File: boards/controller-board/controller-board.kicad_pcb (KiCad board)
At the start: 2 copper layers, 130 x 115 mm, 172 parts, among them J1 Conn_01x02, J2 Conn_01x02, J3 Conn_01x02, J4 Conn_01x02, J5 Conn_01x03, J6 Conn_01x02, Q1 Goford_G11S_20V_11A, Q2 PMV45EN, SW1 EG1271, U1 CAT4201, U10 CAT4201, U11 CAT4201, U12 CAT4201, U13 CAT4201, U14 CAT4201, U15 CAT4201, U17 CAT4201, U18 CAT4201, U25 RPi_Pico, U3 LTC3624, U4 CAT4201, U5 CAT4201, U6 CAT4201, U7 MCP4728, U8 ADS1015IRUGR, U9 ADS1015IRUGR

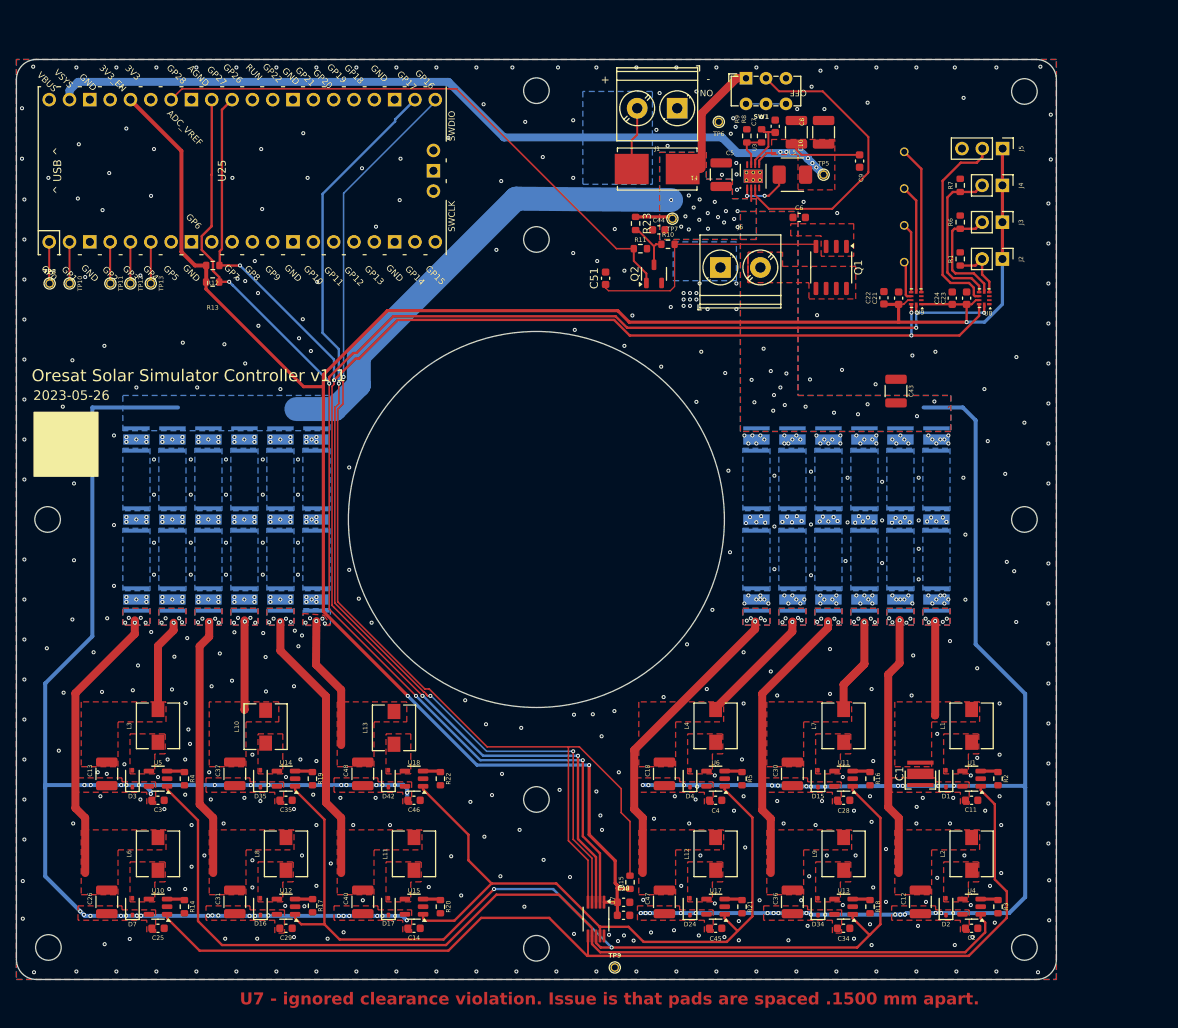
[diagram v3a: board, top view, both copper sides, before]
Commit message: redesigned pcb
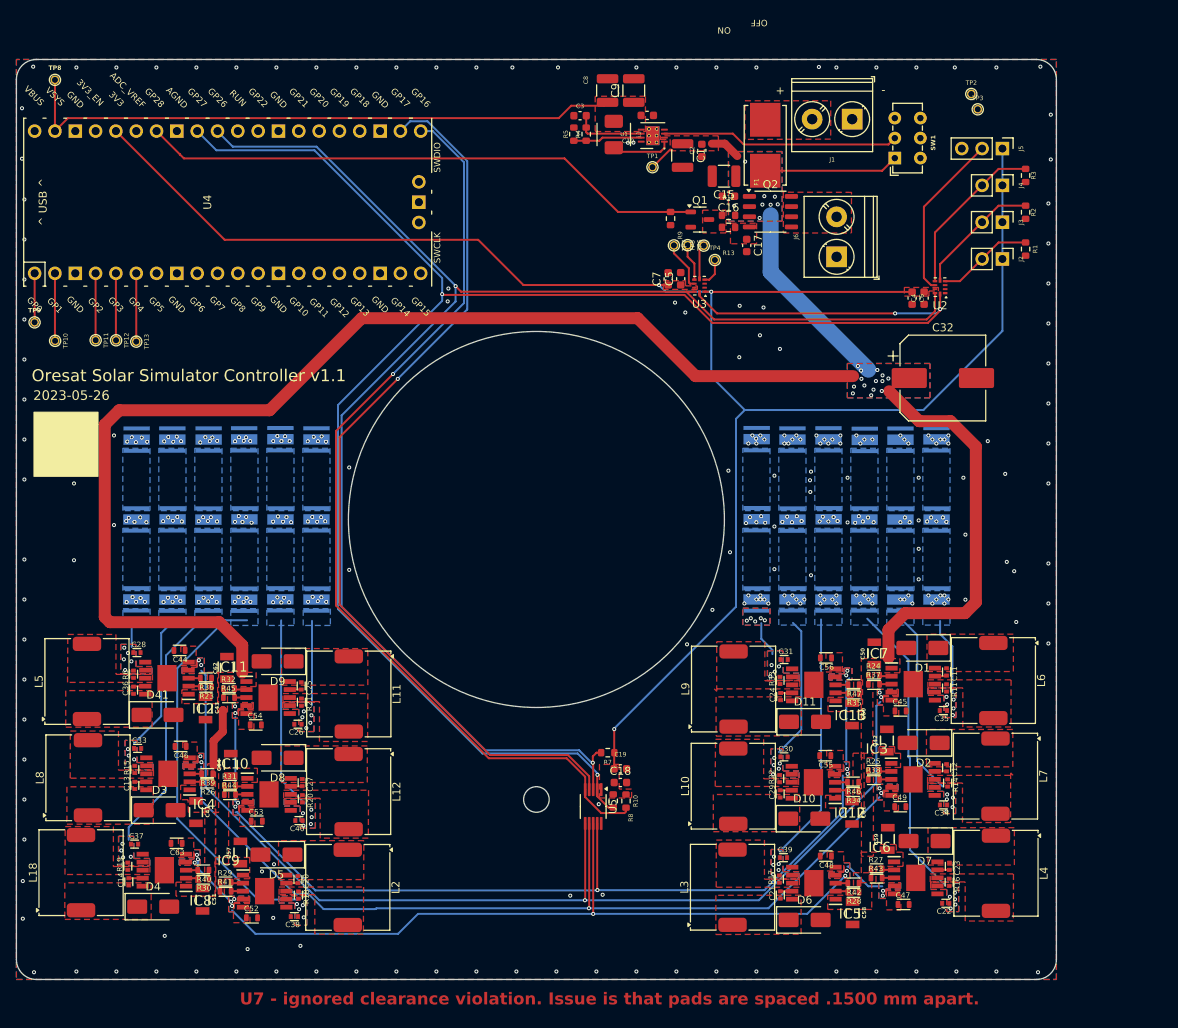
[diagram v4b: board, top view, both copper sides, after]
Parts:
- removed D12, D13, D14: XPEBGR-L1-0000-00D01, oresat-diodes:Cree-LED
- removed D15, D16, D17, D24, D34, D35, D42: NSR0320, Diode_SMD:D_SOD-323
- removed D18, D19, D20, D21: ELUA3535OGB-P6070U23240500-VD1M, oresat-diodes:Cree-LED
- removed D22, D23: NP, oresat-diodes:Cree-LED
- removed D25, D26, D27: XPEBRD-L1-0000-00501, oresat-diodes:Cree-LED
- removed D28, D29, D30, D31, D32, D33, D36, D37, D38, D39, D40: XPEBBL-L1-0000-00201, oresat-diodes:Cree-LED
- removed D43, D44, D45, D46: ELUC3535NUB-P7085Q15070100-S22Q, oresat-diodes:Cree-LED
- removed L13: 56u, Inductor_SMD:L_Wuerth_HCI-5040
- removed the REF** at (206.0, 102.5)
- removed the REF** at (206.0, 49.0)
- removed the REF** at (83.9, 102.5)
- removed the REF** at (84.0, 156.0)
- removed the REF** at (145.0, 156.1)
- removed the REF** at (145.0, 48.9)
- removed the REF** at (145.0, 67.5)
- removed the REF** at (206.0, 156.0)
- removed U10, U11, U12, U13, U14, U15, U17, U18, U6: CAT4201, Package_TO_SOT_SMD:TSOT-23-5
- removed U25: RPi_Pico, oresat-misc:RPi_Pico_TH
- removed U7: MCP4728, Package_SO:MSOP-10_3x3mm_P0.5mm
- removed U8, U9: ADS1015IRUGR, Package_DFN_QFN:Texas_R-PUQFN-N10
- added C15: 22u, Capacitor_SMD:C_1210_3225Metric, F.Cu at (168.5, 59.6)
- added C16: 1u, Capacitor_SMD:C_0603_1608Metric, F.Cu at (169.0, 62.1)
- added C17: C_Small, Capacitor_SMD:C_0603_1608Metric, F.Cu at (171.3, 68.2)
- added C27: 100n, oresat-passives:0402-C, F.Cu at (115.7, 135.4)
- added C32: 470u, Capacitor_SMD:CP_Elec_10x12.5, F.Cu at (195.8, 84.8)
- added C33: 100n, oresat-passives:0402-C, F.Cu at (95.2, 131.1)
- added C38: 100n, oresat-passives:0402-C, F.Cu at (114.7, 152.1)
- added C39: 100n, oresat-passives:0402-C, F.Cu at (175.9, 144.8)
- added C41: 10u, oresat-passives:1206-C, F.Cu at (102.5, 139.1)
- added C42: 10u, oresat-passives:1206-C, F.Cu at (188.8, 130.1)
- added C49: 1u, oresat-passives:0603-C, F.Cu at (190.5, 138.4)
- added C50: 10u, oresat-passives:1206-C, F.Cu at (187.2, 119.2)
- added C52: 1u, oresat-passives:0603-C, F.Cu at (109.4, 152.3)
- added C53: 1u, oresat-passives:0603-C, F.Cu at (110.0, 140.2)
- added C54: 1u, oresat-passives:0603-C, F.Cu at (109.9, 128.2)
- added C55: 1u, oresat-passives:0603-C, F.Cu at (181.1, 132.0)
- added C56: 1u, oresat-passives:0603-C, F.Cu at (181.2, 119.8)
- added C57: 10u, oresat-passives:1206-C, F.Cu at (108.0, 144.1)
- added C58: 10u, oresat-passives:1206-C, F.Cu at (184.5, 151.7)
- added C59: 10u, oresat-passives:1206-C, F.Cu at (188.9, 142.4)
- added C60: 10u, oresat-passives:1206-C, F.Cu at (184.5, 126.9)
- added C61: 10u, oresat-passives:1206-C, F.Cu at (184.5, 139.2)
- added C62: 10u, oresat-passives:1206-C, F.Cu at (106.3, 121.0)
- added C63: 1u, oresat-passives:0603-C, F.Cu at (100.0, 143.0)
- added C64: 10u, oresat-passives:1206-C, F.Cu at (106.8, 133.2)
- added D49: XPEBBL-L1-0000-00201, oresat-diodes:Cree-LED, B.Cu at (190.5, 112.5)
- added D50: XPEBBL-L1-0000-00201, oresat-diodes:Cree-LED, B.Cu at (190.5, 92.5)
- added D51: XPEBBL-L1-0000-00201, oresat-diodes:Cree-LED, B.Cu at (99.5, 112.5)
- added D52: XPEBBL-L1-0000-00201, oresat-diodes:Cree-LED, B.Cu at (99.5, 92.5)
- added D53: XPEBBL-L1-0000-00201, oresat-diodes:Cree-LED, B.Cu at (181.5, 112.5)
- added D54: XPEBBL-L1-0000-00201, oresat-diodes:Cree-LED, B.Cu at (181.5, 92.5)
- added D55: XPEBBL-L1-0000-00201, oresat-diodes:Cree-LED, B.Cu at (186.0, 112.5)
- added D56: XPEBBL-L1-0000-00201, oresat-diodes:Cree-LED, B.Cu at (186.1, 92.5)
- added D57: XPEBBL-L1-0000-00201, oresat-diodes:Cree-LED, B.Cu at (195.0, 112.5)
- added D58: XPEBBL-L1-0000-00201, oresat-diodes:Cree-LED, B.Cu at (195.0, 92.5)
- added D59: XPEBBL-L1-0000-00201, oresat-diodes:Cree-LED, B.Cu at (95.0, 102.5)
- added D60: XPEBBL-L1-0000-00201, oresat-diodes:Cree-LED, B.Cu at (190.5, 102.5)
- added D61: XPEBBL-L1-0000-00201, oresat-diodes:Cree-LED, B.Cu at (99.5, 102.5)
- added D62: XPEBBL-L1-0000-00201, oresat-diodes:Cree-LED, B.Cu at (181.5, 102.5)
- added D63: XPEBBL-L1-0000-00201, oresat-diodes:Cree-LED, B.Cu at (186.0, 102.5)
- added D64: XPEBBL-L1-0000-00201, oresat-diodes:Cree-LED, B.Cu at (195.0, 102.5)
- added D71: XPEBBL-L1-0000-00201, oresat-diodes:Cree-LED, B.Cu at (104.0, 112.5)
- added D72: XPEBBL-L1-0000-00201, oresat-diodes:Cree-LED, B.Cu at (104.0, 92.5)
- added D73: XPEBBL-L1-0000-00201, oresat-diodes:Cree-LED, B.Cu at (108.5, 112.5)
- added D74: XPEBBL-L1-0000-00201, oresat-diodes:Cree-LED, B.Cu at (108.5, 92.5)
- added D75: XPEBBL-L1-0000-00201, oresat-diodes:Cree-LED, B.Cu at (113.0, 112.5)
- added D76: XPEBBL-L1-0000-00201, oresat-diodes:Cree-LED, B.Cu at (113.0, 92.5)
- added D77: XPEBBL-L1-0000-00201, oresat-diodes:Cree-LED, B.Cu at (117.5, 112.5)
- added D78: XPEBBL-L1-0000-00201, oresat-diodes:Cree-LED, B.Cu at (117.5, 92.5)
- added D79: XPEBBL-L1-0000-00201, oresat-diodes:Cree-LED, B.Cu at (177.0, 112.5)
- added D80: XPEBBL-L1-0000-00201, oresat-diodes:Cree-LED, B.Cu at (177.0, 92.5)
- added D81: XPEBBL-L1-0000-00201, oresat-diodes:Cree-LED, B.Cu at (172.5, 112.5)
- added D82: XPEBBL-L1-0000-00201, oresat-diodes:Cree-LED, B.Cu at (172.5, 92.5)
- added D83: XPEBBL-L1-0000-00201, oresat-diodes:Cree-LED, B.Cu at (104.0, 102.5)
- added D84: XPEBBL-L1-0000-00201, oresat-diodes:Cree-LED, B.Cu at (108.5, 102.5)
- added D85: XPEBBL-L1-0000-00201, oresat-diodes:Cree-LED, B.Cu at (113.0, 102.5)
- added D86: XPEBBL-L1-0000-00201, oresat-diodes:Cree-LED, B.Cu at (117.5, 102.5)
- added D87: XPEBBL-L1-0000-00201, oresat-diodes:Cree-LED, B.Cu at (177.0, 102.5)
- added D88: XPEBBL-L1-0000-00201, oresat-diodes:Cree-LED, B.Cu at (172.5, 102.5)
- added IC10: A6214KLKTR-T, oresat-ics:SOP100P600X165-11N, F.Cu at (111.6, 136.9)
- added IC11: A6214KLKTR-T, oresat-ics:SOP100P600X165-11N, F.Cu at (111.5, 124.8)
- added IC12: A6214KLKTR-T, oresat-ics:SOP100P600X165-11N, F.Cu at (179.6, 135.4)
- added IC13: A6214KLKTR-T, oresat-ics:SOP100P600X165-11N, F.Cu at (179.7, 123.2)
- added IC2: A6214KLKTR-T, oresat-ics:SOP100P600X165-11N, F.Cu at (98.8, 122.3)
- added IC3: A6214KLKTR-T, oresat-ics:SOP100P600X165-11N, F.Cu at (192.1, 135.0)
- added IC4: A6214KLKTR-T, oresat-ics:SOP100P600X165-11N, F.Cu at (99.0, 134.3)
- added IC5: A6214KLKTR-T, oresat-ics:SOP100P600X165-11N, F.Cu at (179.7, 148.0)
- added IC6: A6214KLKTR-T, oresat-ics:SOP100P600X165-11N, F.Cu at (192.4, 147.3)
- added IC7: A6214KLKTR-T, oresat-ics:SOP100P600X165-11N, F.Cu at (192.1, 123.1)
- added IC8: A6214KLKTR-T, oresat-ics:SOP100P600X165-11N, F.Cu at (98.5, 146.3)
- added IC9: A6214KLKTR-T, oresat-ics:SOP100P600X165-11N, F.Cu at (111.0, 149.0)
- added L18: 47u, Inductor_SMD:L_Coilcraft_MSS1048-XXX, F.Cu at (88.1, 146.6)
- added R24: 95.3k, oresat-passives:0603-C, F.Cu at (187.2, 122.0)
- added R25: 95.3k, oresat-passives:0603-C, F.Cu at (187.2, 133.9)
- added R26: 95.3k, oresat-passives:0603-C, F.Cu at (103.8, 135.4)
- added R27: 95.3k, oresat-passives:0603-C, F.Cu at (187.5, 146.2)
- added R28: 95.3k, oresat-passives:0603-C, F.Cu at (184.6, 149.1)
- added R29: 95.3k, oresat-passives:0603-C, F.Cu at (106.1, 147.8)
- added R30: 95.3k, oresat-passives:0603-C, F.Cu at (103.4, 147.4)
- added R31: 95.3k, oresat-passives:0603-C, F.Cu at (106.7, 135.8)
- added R32: 95.3k, oresat-passives:0603-C, F.Cu at (106.6, 123.7)
- added R33: .560, oresat-passives:0402-C, F.Cu at (175.5, 122.6)
- added R34: 95.3k, oresat-passives:0603-C, F.Cu at (184.6, 136.5)
- added R35: 95.3k, oresat-passives:0603-C, F.Cu at (184.6, 124.3)
- added R36: 1k, oresat-passives:0603-C, F.Cu at (103.7, 122.3)
- added R37: 1k, oresat-passives:0603-C, F.Cu at (187.2, 123.1)
- added R38: 1k, oresat-passives:0603-C, F.Cu at (187.2, 135.0)
- added R39: 1k, oresat-passives:0603-C, F.Cu at (103.8, 134.3)
- added R40: 1k, oresat-passives:0603-C, F.Cu at (103.4, 146.3)
- added R41: 1k, oresat-passives:0603-C, F.Cu at (106.1, 149.0)
- added R42: 1k, oresat-passives:0603-C, F.Cu at (184.6, 148.0)
- added R43: 1k, oresat-passives:0603-C, F.Cu at (187.5, 147.3)
- added R44: 1k, oresat-passives:0603-C, F.Cu at (106.7, 136.9)
- added R45: 1k, oresat-passives:0603-C, F.Cu at (106.6, 124.8)
- added R46: 1k, oresat-passives:0603-C, F.Cu at (184.6, 135.4)
- added R47: 1k, oresat-passives:0603-C, F.Cu at (184.6, 123.2)
- added U2: ADS1015IRUGR, Package_DFN_QFN:Texas_R-PUQFN-N10, F.Cu at (195.5, 73.5)
- C1: footprint oresat-diodes:Cree-LED -> Capacitor_SMD:C_1210_3225Metric
- C10: value 2u2 -> 100n
- C11, C14, C25, C28, C29, C34, C35: value 4.7u -> 100n; footprint Capacitor_SMD:C_0603_1608Metric -> oresat-passives:0402-C
- C12, C13, C26, C30, C31, C36, C37, C40: value 22u -> 100n; footprint Capacitor_SMD:C_1210_3225Metric -> oresat-passives:0402-C
- C18, C5: value 22u -> 1u; footprint Capacitor_SMD:C_1210_3225Metric -> Capacitor_SMD:C_0603_1608Metric
- C2: value 4.7u -> 100n
- C20, C21, C23: value 1u -> 100n; footprint Capacitor_SMD:C_0603_1608Metric -> oresat-passives:0402-C
- C22, C24: footprint Capacitor_SMD:C_0603_1608Metric -> oresat-passives:0402-C
- C3: value 4.7u -> 2u2
- C4: value 4.7u -> 1u
- C43: value 22u -> 10u; footprint Capacitor_SMD:C_1210_3225Metric -> oresat-passives:1206-C
- C44: footprint Capacitor_SMD:C_0603_1608Metric -> oresat-passives:0603-C
- C45, C46: value 4.7u -> 1u; footprint Capacitor_SMD:C_0603_1608Metric -> oresat-passives:0603-C
- C47, C48: value 22u -> 1u; footprint Capacitor_SMD:C_1210_3225Metric -> oresat-passives:0603-C
- C51: value C_Small -> 10u; footprint Capacitor_SMD:C_0603_1608Metric -> oresat-passives:1206-C
- C7: value 22u -> 100n; footprint Capacitor_SMD:C_1210_3225Metric -> Capacitor_SMD:C_0603_1608Metric
- C9: value 100n -> 22u; footprint Capacitor_SMD:C_0603_1608Metric -> Capacitor_SMD:C_1210_3225Metric
- D1, D2, D3, D4, D7: value NSR0320 -> VS-10MQ060NTRPBF; footprint Diode_SMD:D_SOD-323 -> Diode_SMD:D_SMA
- D10, D11, D9: value XPEBGR-L1-0000-00D01 -> VS-10MQ060NTRPBF; footprint oresat-diodes:Cree-LED -> Diode_SMD:D_SMA; moved to F.Cu
- D41: value XPEBBL-L1-0000-00201 -> VS-10MQ060NTRPBF; footprint oresat-diodes:Cree-LED -> Diode_SMD:D_SMA; moved to F.Cu
- D47, D48: value NP -> XPEBBL-L1-0000-00201
- D5, D6, D8: value XPEBRD-L1-0000-00501 -> VS-10MQ060NTRPBF; footprint oresat-diodes:Cree-LED -> Diode_SMD:D_SMA; moved to F.Cu
- L1: value 56u -> 3u3; footprint Inductor_SMD:L_Wuerth_HCI-5040 -> oresat-passives:L_ECS-MPI4040
- L10, L11, L12, L2, L3, L4, L6, L7, L8, L9: value 56u -> 47u; footprint Inductor_SMD:L_Wuerth_HCI-5040 -> Inductor_SMD:L_Coilcraft_MSS1048-XXX
- L5: value 3u3 -> 47u; footprint oresat-passives:L_ECS-MPI4040 -> Inductor_SMD:L_Coilcraft_MSS1048-XXX
- Q1: value Goford_G11S_20V_11A -> PMV45EN; footprint Package_SO:SOP-8_3.9x4.9mm_P1.27mm -> Package_TO_SOT_SMD:SOT-23-3
- Q2: value PMV45EN -> Goford_G11S_20V_11A; footprint Package_TO_SOT_SMD:SOT-23-3 -> Package_SO:SOP-8_3.9x4.9mm_P1.27mm
- R10: value 0 -> 100k
- R11, R14, R16, R17, R18, R19, R20, R21, R22, R6: value 10k -> .560; footprint Resistor_SMD:R_0603_1608Metric -> oresat-passives:0402-C
- R12: value 4.7k -> 1k
- R13: value 4.7k -> 0
- R15: value 100k -> .560; footprint Resistor_SMD:R_0603_1608Metric -> oresat-passives:0402-C
- R23: value 1k -> 95.3k; footprint Resistor_SMD:R_0603_1608Metric -> oresat-passives:0603-C
- R4, R5: value 10k -> 100k
- R7: value 10k -> 4.7k
- R8: value 100k -> 4.7k
- R9: value 100k -> 10k
- TP1, TP2, TP3, TP4: moved to F.Cu
- U1: value CAT4201 -> LTC3624; footprint Package_TO_SOT_SMD:TSOT-23-5 -> oresat-ics:DFN-8-1EP_3x3mm_P0.5mm_EP1.65x2.38mm_ThermalVias0.3mm
- U3: value LTC3624 -> ADS1015IRUGR; footprint oresat-ics:DFN-8-1EP_3x3mm_P0.5mm_EP1.65x2.38mm_ThermalVias0.3mm -> Package_DFN_QFN:Texas_R-PUQFN-N10
- U4: value CAT4201 -> RPi_Pico; footprint Package_TO_SOT_SMD:TSOT-23-5 -> oresat-misc:RPi_Pico_TH
- U5: value CAT4201 -> MCP4728; footprint Package_TO_SOT_SMD:TSOT-23-5 -> Package_SO:MSOP-10_3x3mm_P0.5mm
- moved U4 128.1 mm to (106.4, 62.8), turned to 90 degrees
- moved R6 117.8 mm to (94.6, 121.8)
- moved L5 108.6 mm to (88.8, 122.8), turned to 90 degrees
- moved TP9 108.5 mm to (82.3, 77.9)
- moved L6 106.6 mm to (202.1, 122.6), turned to -90 degrees
- moved C2 102.9 mm to (165.7, 56.4), turned to -90 degrees
- moved C3 100.5 mm to (150.5, 52.0), turned to 180 degrees
- moved D7 99.4 mm to (193.5, 142.7), turned to 180 degrees
- moved D6 97.4 mm to (178.5, 152.6), turned to 0 degrees
- moved R14 96.6 mm to (196.4, 135.4)
- moved C43 95.0 mm to (103.6, 126.1), turned to -90 degrees
- moved R4 94.9 mm to (151.2, 54.3), turned to 90 degrees
- moved C51 92.6 mm to (103.3, 150.0), turned to -90 degrees
- moved R3 91.5 mm to (206.2, 59.5)
- moved C28 90.2 mm to (95.1, 119.1)
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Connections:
- C1 pad 2: Net-(D26-K) -> GND
- C10 pad 1: Net-(U3-INTVcc) -> +5V
- C11 pad 1: VCC -> Net-(D1-K)
- C11 pad 2: GND -> Net-(IC7-BOOT)
- C12 pad 1: VCC -> Net-(D2-K)
- C12 pad 2: Net-(D12-K) -> Net-(IC3-BOOT)
- C13 pad 1: VCC -> Net-(D3-K)
- C13 pad 2: Net-(D10-K) -> Net-(IC4-BOOT)
- C14 pad 1: VCC -> Net-(D4-K)
- C14 pad 2: GND -> Net-(IC8-BOOT)
- C18 pad 1: VCC -> +3.3V
- C18 pad 2: Net-(D21-K) -> GND
- C20 pad 1: +3.3V -> Net-(D5-K)
- C20 pad 2: GND -> Net-(IC9-BOOT)
- C21 pad 1: +3.3V -> Net-(D6-K)
- C21 pad 2: GND -> Net-(IC5-BOOT)
- C22 pad 1: +3.3V -> Net-(D55-A)
- C23 pad 1: +3.3V -> Net-(D7-K)
- C23 pad 2: GND -> Net-(IC6-BOOT)
- C24 pad 1: +3.3V -> Net-(D11-K)
- C24 pad 2: GND -> Net-(IC13-BOOT)
- C25 pad 1: VCC -> Net-(D9-K)
- C25 pad 2: GND -> Net-(IC11-BOOT)
- C26 pad 1: VCC -> Net-(D77-A)
- C26 pad 2: Net-(D8-K) -> GND
- C28 pad 1: VCC -> Net-(D47-A)
- C29 pad 1: VCC -> Net-(D10-K)
- C29 pad 2: GND -> Net-(IC12-BOOT)
- C3 pad 1: VCC -> Net-(U1-INTVcc)
- C30 pad 1: VCC -> Net-(D79-A)
- C30 pad 2: Net-(D31-K) -> GND
- C31 pad 1: VCC -> Net-(D81-A)
- C31 pad 2: Net-(D29-K) -> GND
- C34 pad 1: VCC -> Net-(D49-A)
- C35 pad 1: VCC -> Net-(D57-A)
- C36 pad 1: VCC -> Net-(D41-K)
- C36 pad 2: Net-(D39-K) -> Net-(IC2-BOOT)
- C37 pad 1: VCC -> Net-(D71-A)
- C37 pad 2: Net-(D37-K) -> GND
- C4 pad 1: VCC -> +3.3V
- C40 pad 1: VCC -> Net-(D75-A)
- C40 pad 2: Net-(D19-K) -> GND
- C44 pad 1: VCC -> Net-(IC2-VCC)
- C45 pad 1: VCC -> Net-(IC7-VCC)
- C46 pad 1: VCC -> Net-(IC4-VCC)
- C47 pad 1: VCC -> Net-(IC6-VCC)
- C47 pad 2: Net-(D46-K) -> GND
- C48 pad 1: VCC -> Net-(IC5-VCC)
- C48 pad 2: Net-(D44-K) -> GND
- C5 pad 1: VCC -> +3.3V
- C51 pad 1: Net-(Q1-G) -> VCC
- C6 pad 1: VCC -> +3.3V
- C7 pad 1: +5V -> +3.3V
- D1 pad 1: VCC -> Net-(D1-K)
- D1 pad 2: Net-(D1-A) -> GND
- D10 pad 2: Net-(D10-A) -> GND
- D11 pad 2: VCC -> GND
- D2 pad 1: VCC -> Net-(D2-K)
- D2 pad 2: Net-(D2-A) -> GND
- D3 pad 1: VCC -> Net-(D3-K)
- D3 pad 2: Net-(D3-A) -> GND
- D4 pad 1: VCC -> Net-(D4-K)
- D4 pad 2: Net-(D4-A) -> GND
- D41 pad 1: Net-(D39-A) -> Net-(D41-K)
- D41 pad 2: Net-(D38-K) -> GND
- D47 pad 2: Net-(D43-K) -> Net-(D47-A)
- D48 pad 1: Net-(D46-A) -> GND
- D5 pad 2: VCC -> GND
- D6 pad 2: Net-(D5-K) -> GND
- D7 pad 1: VCC -> Net-(D7-K)
- D7 pad 2: Net-(D7-A) -> GND
- D8 pad 2: Net-(D6-K) -> GND
- D9 pad 1: Net-(D13-A) -> Net-(D9-K)
- D9 pad 2: VCC -> GND
- L1 pad 1: Net-(D1-A) -> Net-(U1-SW)
- L1 pad 2: Net-(D26-K) -> +5V
- L10 pad 1: Net-(D35-A) -> Net-(D10-K)
- L10 pad 2: Net-(D37-K) -> Net-(IC12-CSH)
- L11 pad 1: Net-(D17-A) -> Net-(D9-K)
- L11 pad 2: Net-(D19-K) -> Net-(IC11-CSH)
- L12 pad 1: Net-(D24-A) -> Net-(D8-K)
- L12 pad 2: Net-(D46-K) -> Net-(IC10-CSH)
- L2 pad 1: Net-(D2-A) -> Net-(D5-K)
- L2 pad 2: Net-(D12-K) -> Net-(IC9-CSH)
- L3 pad 1: Net-(D3-A) -> Net-(D6-K)
- L3 pad 2: Net-(D10-K) -> Net-(IC5-CSH)
- L4 pad 1: Net-(D4-A) -> Net-(D7-K)
- L4 pad 2: Net-(D21-K) -> Net-(IC6-CSH)
- L5 pad 1: Net-(U3-SW) -> Net-(D41-K)
- L5 pad 2: +5V -> Net-(IC2-CSH)
- L6 pad 1: Net-(D7-A) -> Net-(D1-K)
- L6 pad 2: Net-(D8-K) -> Net-(IC7-CSH)
- L7 pad 1: Net-(D15-A) -> Net-(D2-K)
- L7 pad 2: Net-(D31-K) -> Net-(IC3-CSH)
- L8 pad 1: Net-(D16-A) -> Net-(D3-K)
- L8 pad 2: Net-(D29-K) -> Net-(IC4-CSH)
- L9 pad 1: Net-(D34-A) -> Net-(D11-K)
- L9 pad 2: Net-(D39-K) -> Net-(IC13-CSH)
- Q1 pad 1: VCC -> /PWM
- Q1 pad 2: VCC -> GND
- Q1 pad 3: VCC -> Net-(Q1-D)
- Q2 pad 1: /PWM -> VCC
- Q2 pad 2: GND -> VCC
- Q2 pad 3: Net-(Q2-D) -> VCC
- R10 pad 1: Net-(Q2-D) -> +3.3V
- R10 pad 2: Net-(Q1-G) -> /DAC_RDY/~{BSY}
- R11 pad 1: /PWM -> Net-(IC7-CSH)
- R11 pad 2: GND -> Net-(D57-A)
- R12 pad 1: +3.3V -> VCC
- R12 pad 2: /SDA1 -> Net-(Q1-D)
- R13 pad 1: +3.3V -> Net-(Q1-D)
- R13 pad 2: /SCL1 -> Net-(Q2-G)
- R14 pad 1: Net-(U10-RSET) -> Net-(IC3-CSH)
- R14 pad 2: GND -> Net-(D49-A)
- R15 pad 1: +3.3V -> Net-(IC4-CSH)
- R15 pad 2: /DAC_RDY/~{BSY} -> Net-(D51-A)
- R16 pad 1: Net-(U11-RSET) -> Net-(IC6-CSH)
- R16 pad 2: GND -> Net-(D55-A)
- R17 pad 1: Net-(U12-RSET) -> Net-(IC5-CSH)
- R17 pad 2: GND -> Net-(D53-A)
- R18 pad 1: Net-(U13-RSET) -> Net-(IC9-CSH)
- R18 pad 2: GND -> Net-(D73-A)
- R19 pad 2: GND -> Net-(D71-A)
- R2 pad 1: Net-(U1-RSET) -> /THERM2
- R20 pad 1: Net-(U15-RSET) -> Net-(IC10-CSH)
- R20 pad 2: GND -> Net-(D75-A)
- R21 pad 1: Net-(U17-RSET) -> Net-(IC11-CSH)
- R21 pad 2: GND -> Net-(D77-A)
- R22 pad 1: Net-(U18-RSET) -> Net-(IC12-CSH)
- R22 pad 2: GND -> Net-(D79-A)
- R23 pad 2: Net-(Q2-D) -> Net-(IC2-TON)
- R3 pad 1: Net-(U4-RSET) -> /THERM3
- R4 pad 1: Net-(U5-RSET) -> Net-(U1-MODE)
- R4 pad 2: GND -> Net-(U1-INTVcc)
- R5 pad 1: Net-(U6-RSET) -> Net-(U1-MODE)
- R6 pad 1: /THERM2 -> Net-(IC2-CSH)
- R6 pad 2: GND -> Net-(D47-A)
- R7 pad 1: /THERM3 -> +3.3V
- R7 pad 2: GND -> /SDA1
- R8 pad 1: Net-(U3-MODE) -> +3.3V
- R8 pad 2: Net-(U3-INTVcc) -> /SCL1
- R9 pad 1: Net-(U3-MODE) -> /PWM
- SW1 pad 4: GND -> (no net)
- SW1 pad 5: GND -> (no net)
- SW1 pad 6: GND -> (no net)
- TP1 pad 1: Net-(U9-AIN0) -> VCC
- TP10 pad 1: Net-(U25-GPIO1) -> Net-(U4-GPIO1)
- TP11 pad 1: Net-(U25-GPIO2) -> Net-(U4-GPIO2)
- TP12 pad 1: Net-(U25-GPIO3) -> Net-(U4-GPIO3)
- TP13 pad 1: Net-(U25-GPIO4) -> Net-(U4-GPIO4)
- TP2 pad 1: Net-(U9-AIN1) -> GND
- TP3 pad 1: Net-(U9-AIN2) -> GND
- TP4 pad 1: Net-(U9-AIN3) -> Net-(U3-AIN0)
- TP5 pad 1: +5V -> Net-(U3-AIN1)
- TP6 pad 1: GND -> Net-(U3-AIN2)
- TP7 pad 1: VCC -> Net-(U3-AIN3)
- TP8 pad 1: Net-(U25-GPIO0) -> +5V
- TP9 pad 1: GND -> Net-(U4-GPIO0)
- U1 pad 1: /RED_LIM -> Net-(U1-SW)
- U1 pad 2: GND -> VCC
- U1 pad 3: Net-(U1-RSET) -> Net-(SW1-B)
- U1 pad 4: Net-(D1-A) -> unconnected-(U1-PGOOD-Pad4)
- U1 pad 5: VCC -> +5V
- U3 pad 1: Net-(U3-SW) -> +3.3V
- U3 pad 2: VCC -> unconnected-(U3-ALERT/RDY-Pad2)
- U3 pad 3: Net-(SW1-B) -> GND
- U3 pad 4: unconnected-(U3-PGOOD-Pad4) -> Net-(U3-AIN0)
- U3 pad 5: +5V -> Net-(U3-AIN1)
- U3 pad 6: Net-(U3-INTVcc) -> Net-(U3-AIN2)
- U3 pad 7: Net-(U3-MODE) -> Net-(U3-AIN3)
- U3 pad 8: GND -> +3.3V
- U3 pad 9: GND -> /SDA1
- U4 pad 1: /GREEN_LIM -> Net-(U4-GPIO0)
- U4 pad 2: GND -> Net-(U4-GPIO1)
- U4 pad 3: Net-(U4-RSET) -> GND
- U4 pad 4: Net-(D2-A) -> Net-(U4-GPIO2)
- U4 pad 5: VCC -> Net-(U4-GPIO3)
- U5 pad 1: /GREEN_LIM -> +3.3V
- U5 pad 2: GND -> /SCL1
- U5 pad 3: Net-(U5-RSET) -> /SDA1
- U5 pad 4: Net-(D3-A) -> /DAC_~{LDAC}
- U5 pad 5: VCC -> /DAC_RDY/~{BSY}
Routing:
- net VCC: track 417.2 -> 253.0 mm, vias 97 -> 22
- net /RED_LIM: track 133.1 -> 0.00 mm
- net RED_LIM: track 0.00 -> 130.5 mm, vias 0 -> 5
- net /GREEN_LIM: track 128.4 -> 0.00 mm
- net /BLUE_LIM: track 125.6 -> 0.00 mm, vias 2 -> 0
- net UV_LIM: track 0.00 -> 118.4 mm, vias 0 -> 9
- net GREEN_LIM: track 0.00 -> 111.1 mm, vias 0 -> 5
- net BLUE_LIM: track 0.00 -> 104.6 mm, vias 0 -> 11
- net /UV_LIM: track 85.3 -> 0.00 mm
- net Net-(D73-A): track 0.00 -> 49.3 mm, vias 0 -> 4
- net Net-(D46-K): track 38.2 -> 0.00 mm, vias 5 -> 0
- net Net-(D55-A): track 0.00 -> 37.3 mm, vias 0 -> 5
- net Net-(D39-K): track 35.3 -> 0.00 mm, vias 5 -> 0
- net Net-(D8-K): track 35.2 -> 0.00 mm, vias 5 -> 0
- net +5V: track 111.9 -> 77.0 mm, vias 5 -> 0
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- added copper zone on F.Cu, net +3.3V
- added copper zone on B.Cu, net BLUE_LIM
- added copper zone on F.Cu, net BLUE_LIM
- added copper zone on B.Cu, net GREEN_LIM
- added copper zone on F.Cu, net GREEN_LIM
- added copper zone on F.Cu, net Net-(D1-K)
- added copper zone on F.Cu, net Net-(D11-K)
- added copper zone on F.Cu, net Net-(D2-K)
- added copper zone on F.Cu, net Net-(D3-K)
- added copper zone on F.Cu, net Net-(D4-K)
- added copper zone on F.Cu, net Net-(D41-K)
- added copper zone on B.Cu, net Net-(D47-A)
- added copper zone on F.Cu, net Net-(D47-A)
- added copper zone on B.Cu, net Net-(D49-A)
- added copper zone on F.Cu, net Net-(D49-A)
- added copper zone on B.Cu, net Net-(D49-K)
- added copper zone on F.Cu, net Net-(D5-K)
- added copper zone on B.Cu, net Net-(D50-A)
- added copper zone on B.Cu, net Net-(D51-A)
- added copper zone on F.Cu, net Net-(D51-A)
- added copper zone on B.Cu, net Net-(D51-K)
- added copper zone on B.Cu, net Net-(D52-A)
- added copper zone on B.Cu, net Net-(D53-A)
- added copper zone on F.Cu, net Net-(D53-A)
- added copper zone on B.Cu, net Net-(D53-K)
- added copper zone on B.Cu, net Net-(D54-A)
- added copper zone on B.Cu, net Net-(D55-A)
- added copper zone on F.Cu, net Net-(D55-A)
- added copper zone on B.Cu, net Net-(D55-K)
- added copper zone on B.Cu, net Net-(D56-A)
- added copper zone on B.Cu, net Net-(D57-A)
- added copper zone on F.Cu, net Net-(D57-A)
- added copper zone on B.Cu, net Net-(D57-K)
- added copper zone on B.Cu, net Net-(D58-A)
- added copper zone on F.Cu, net Net-(D6-K)
- added copper zone on F.Cu, net Net-(D7-K)
- added copper zone on B.Cu, net Net-(D71-A)
- added copper zone on F.Cu, net Net-(D71-A)
- added copper zone on B.Cu, net Net-(D71-K)
- added copper zone on B.Cu, net Net-(D72-A)
- added copper zone on B.Cu, net Net-(D73-A)
- added copper zone on F.Cu, net Net-(D73-A)
- added copper zone on B.Cu, net Net-(D73-K)
- added copper zone on B.Cu, net Net-(D74-A)
- added copper zone on B.Cu, net Net-(D75-A)
- added copper zone on F.Cu, net Net-(D75-A)
- added copper zone on B.Cu, net Net-(D75-K)
- added copper zone on B.Cu, net Net-(D76-A)
- added copper zone on B.Cu, net Net-(D77-A)
- added copper zone on F.Cu, net Net-(D77-A)
- added copper zone on B.Cu, net Net-(D77-K)
- added copper zone on B.Cu, net Net-(D78-A)
- added copper zone on B.Cu, net Net-(D79-A)
- added copper zone on F.Cu, net Net-(D79-A)
- added copper zone on B.Cu, net Net-(D79-K)
- added copper zone on B.Cu, net Net-(D80-A)
- added copper zone on B.Cu, net Net-(D81-A)
- added copper zone on F.Cu, net Net-(D81-A)
- added copper zone on B.Cu, net Net-(D81-K)
- added copper zone on B.Cu, net Net-(D82-A)
- added copper zone on F.Cu, net Net-(D9-K)
- added copper zone on F.Cu, net Net-(IC10-CSH)
- added copper zone on F.Cu, net Net-(IC10-VCC)
- added copper zone on F.Cu, net Net-(IC11-CSH)
- added copper zone on F.Cu, net Net-(IC11-VCC)
- added copper zone on F.Cu, net Net-(IC12-CSH)
- added copper zone on F.Cu, net Net-(IC12-VCC)
- added copper zone on F.Cu, net Net-(IC13-CSH)
- added copper zone on F.Cu, net Net-(IC13-VCC)
- added copper zone on F.Cu, net Net-(IC2-CSH)
- added copper zone on F.Cu, net Net-(IC2-VCC)
- added copper zone on F.Cu, net Net-(IC3-CSH)
- added copper zone on F.Cu, net Net-(IC3-VCC)
- added copper zone on F.Cu, net Net-(IC4-CSH)
- added copper zone on F.Cu, net Net-(IC4-VCC)
- added copper zone on F.Cu, net Net-(IC5-CSH)
- added copper zone on F.Cu, net Net-(IC5-VCC)
- added copper zone on F.Cu, net Net-(IC6-CSH)
- added copper zone on F.Cu, net Net-(IC6-VCC)
- added copper zone on F.Cu, net Net-(IC7-CSH)
- added copper zone on F.Cu, net Net-(IC7-VCC)
- added copper zone on F.Cu, net Net-(IC8-CSH)
- added copper zone on F.Cu, net Net-(IC8-VCC)
- added copper zone on F.Cu, net Net-(IC9-CSH)
- added copper zone on F.Cu, net Net-(IC9-VCC)
- added copper zone on F.Cu, net Net-(J1-Pin_2)
- added copper zone on F.Cu, net Net-(Q1-D)
- added copper zone on F.Cu, net Net-(Q2-G)
- added copper zone on B.Cu, net RED_LIM
- added copper zone on F.Cu, net RED_LIM
- added copper zone on B.Cu, net UV_LIM
- added copper zone on F.Cu, net UV_LIM
- removed copper zone on F.Cu, net Net-(D1-A)
- removed copper zone on B.Cu, net Net-(D10-A)
- removed copper zone on B.Cu, net Net-(D10-K)
- removed copper zone on B.Cu, net Net-(D11-K)
- removed copper zone on B.Cu, net Net-(D12-A)
- removed copper zone on B.Cu, net Net-(D12-K)
- removed copper zone on F.Cu, net Net-(D12-K)
- removed copper zone on B.Cu, net Net-(D13-A)
- removed copper zone on F.Cu, net Net-(D15-A)
- removed copper zone on F.Cu, net Net-(D16-A)
- removed copper zone on F.Cu, net Net-(D17-A)
- removed copper zone on B.Cu, net Net-(D18-K)
- removed copper zone on B.Cu, net Net-(D19-A)
- removed copper zone on B.Cu, net Net-(D19-K)
- removed copper zone on F.Cu, net Net-(D19-K)
- removed copper zone on F.Cu, net Net-(D2-A)
- removed copper zone on B.Cu, net Net-(D20-K)
- removed copper zone on B.Cu, net Net-(D21-A)
- removed copper zone on B.Cu, net Net-(D21-K)
- removed copper zone on F.Cu, net Net-(D21-K)
- removed copper zone on F.Cu, net Net-(D24-A)
- removed copper zone on B.Cu, net Net-(D25-K)
- removed copper zone on B.Cu, net Net-(D26-A)
- removed copper zone on B.Cu, net Net-(D26-K)
- removed copper zone on F.Cu, net Net-(D26-K)
- removed copper zone on B.Cu, net Net-(D28-K)
- removed copper zone on B.Cu, net Net-(D29-A)
- removed copper zone on B.Cu, net Net-(D29-K)
- removed copper zone on F.Cu, net Net-(D29-K)
- removed copper zone on F.Cu, net Net-(D3-A)
- removed copper zone on B.Cu, net Net-(D30-K)
- removed copper zone on B.Cu, net Net-(D31-A)
- removed copper zone on B.Cu, net Net-(D31-K)
- removed copper zone on F.Cu, net Net-(D31-K)
- removed copper zone on F.Cu, net Net-(D34-A)
- removed copper zone on F.Cu, net Net-(D35-A)
- removed copper zone on B.Cu, net Net-(D36-K)
- removed copper zone on B.Cu, net Net-(D37-A)
- removed copper zone on B.Cu, net Net-(D37-K)
- removed copper zone on F.Cu, net Net-(D37-K)
- removed copper zone on B.Cu, net Net-(D38-K)
- removed copper zone on B.Cu, net Net-(D39-A)
- removed copper zone on B.Cu, net Net-(D39-K)
- removed copper zone on F.Cu, net Net-(D39-K)
- removed copper zone on F.Cu, net Net-(D4-A)
- removed copper zone on F.Cu, net Net-(D42-A)
- removed copper zone on B.Cu, net Net-(D43-K)
- removed copper zone on B.Cu, net Net-(D44-K)
- removed copper zone on F.Cu, net Net-(D44-K)
- removed copper zone on B.Cu, net Net-(D46-A)
- removed copper zone on B.Cu, net Net-(D46-K)
- removed copper zone on F.Cu, net Net-(D46-K)
- removed copper zone on B.Cu, net Net-(D5-K)
- removed copper zone on B.Cu, net Net-(D6-K)
- removed copper zone on F.Cu, net Net-(D7-A)
- removed copper zone on B.Cu, net Net-(D8-K)
- removed copper zone on B.Cu, net Net-(J1-Pin_2)

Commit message: changed footprint on sense resistors, adjusted traces
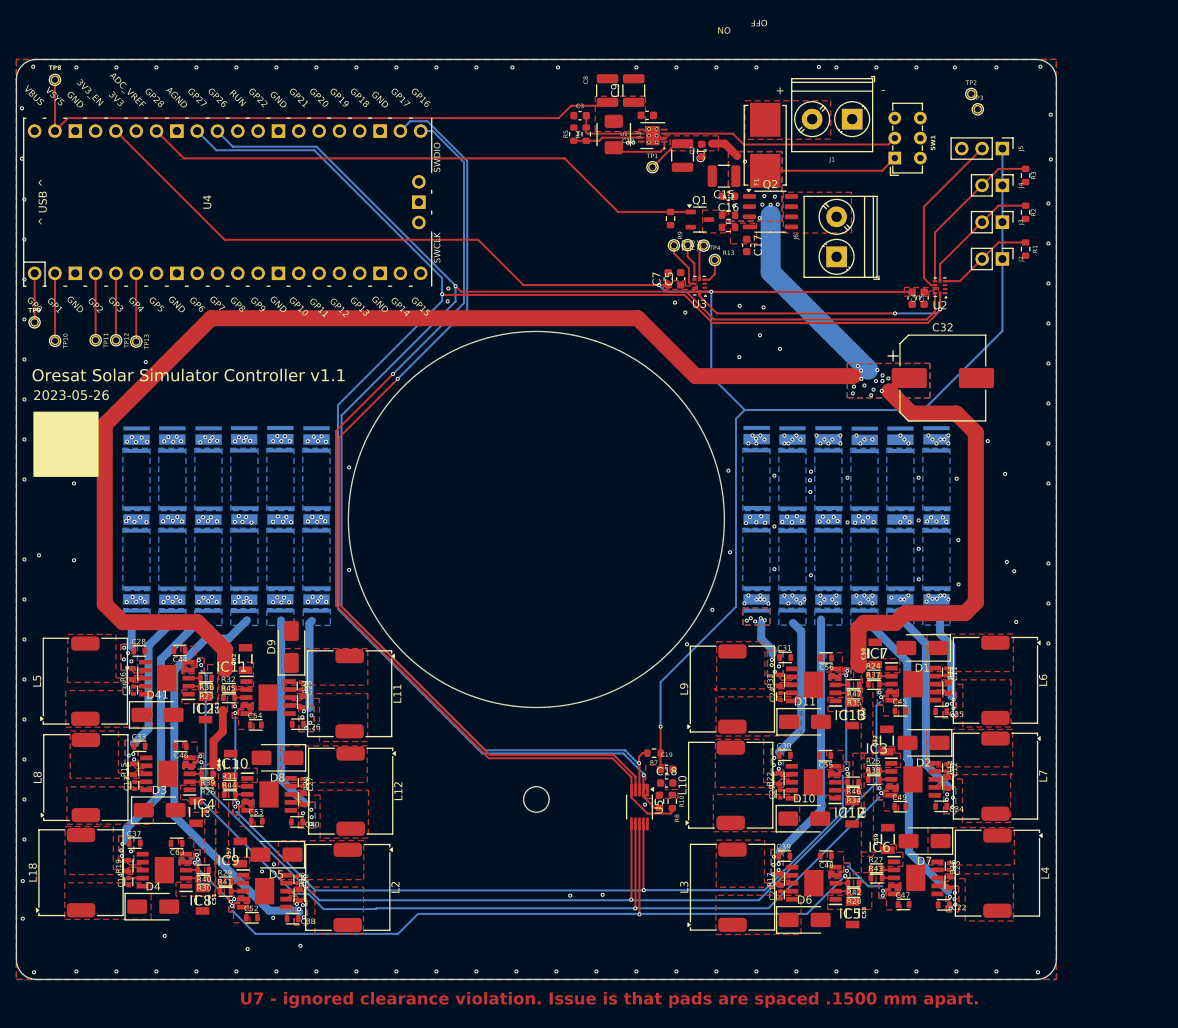
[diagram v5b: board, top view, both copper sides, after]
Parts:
- C22, C26, C28, C30, C31, C33, C34, C35, C37, C38, C39, C40: footprint oresat-passives:0402-C -> oresat-passives:0603-C
- R11, R14, R15, R16, R17, R18, R19, R20, R21, R22, R33, R6: value .560 -> .576; footprint oresat-passives:0402-C -> oresat-passives:0603-C
- moved R10 5.79 mm to (162.0, 137.8)
- moved R7 5.79 mm to (159.7, 131.7)
- moved C18 5.79 mm to (161.3, 135.4)
- moved C19 5.79 mm to (161.3, 133.7)
- moved R8 5.79 mm to (160.4, 137.7)
- moved U5 5.79 mm to (157.9, 138.4)
- moved C62 2.57 mm to (108.6, 119.9)
- moved D9 2.51 mm to (114.4, 118.4), turned to 90 degrees
- moved C33 0.36 mm to (95.4, 130.8)
- moved C28 0.35 mm to (95.4, 118.9)
- moved L10 0.34 mm to (169.3, 135.7)
- moved C34 0.34 mm to (195.6, 138.4)
- moved C38 0.33 mm to (114.5, 152.4)
- moved C22 0.32 mm to (195.9, 150.7)
- moved C35 0.31 mm to (195.6, 126.5)
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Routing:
- net /SCL1: track 229.6 -> 235.5 mm
- net /DAC_RDY/~{BSY}: track 118.1 -> 123.9 mm
- net /DAC_~{LDAC}: track 114.7 -> 120.5 mm
- net /SDA1: track 194.0 -> 199.8 mm
- net VCC: track 253.0 -> 256.7 mm
- net Net-(D73-A): track 49.3 -> 52.6 mm
- net Net-(IC8-CSH): track 0.00 -> 2.50 mm
- net Net-(D77-A): track 10.5 -> 12.9 mm
- net +3.3V: track 237.2 -> 234.8 mm
- net Net-(D49-A): track 22.9 -> 25.2 mm, vias 5 -> 4
- net Net-(D55-A): track 37.3 -> 39.7 mm
- net Net-(D53-A): track 31.2 -> 33.4 mm
- net Net-(IC5-CSH): track 0.00 -> 2.24 mm
- net Net-(IC12-CSH): track 0.00 -> 2.23 mm
- net Net-(IC6-CSH): track 0.00 -> 2.19 mm
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
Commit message: minor changes to tracks and zones on controller pcb
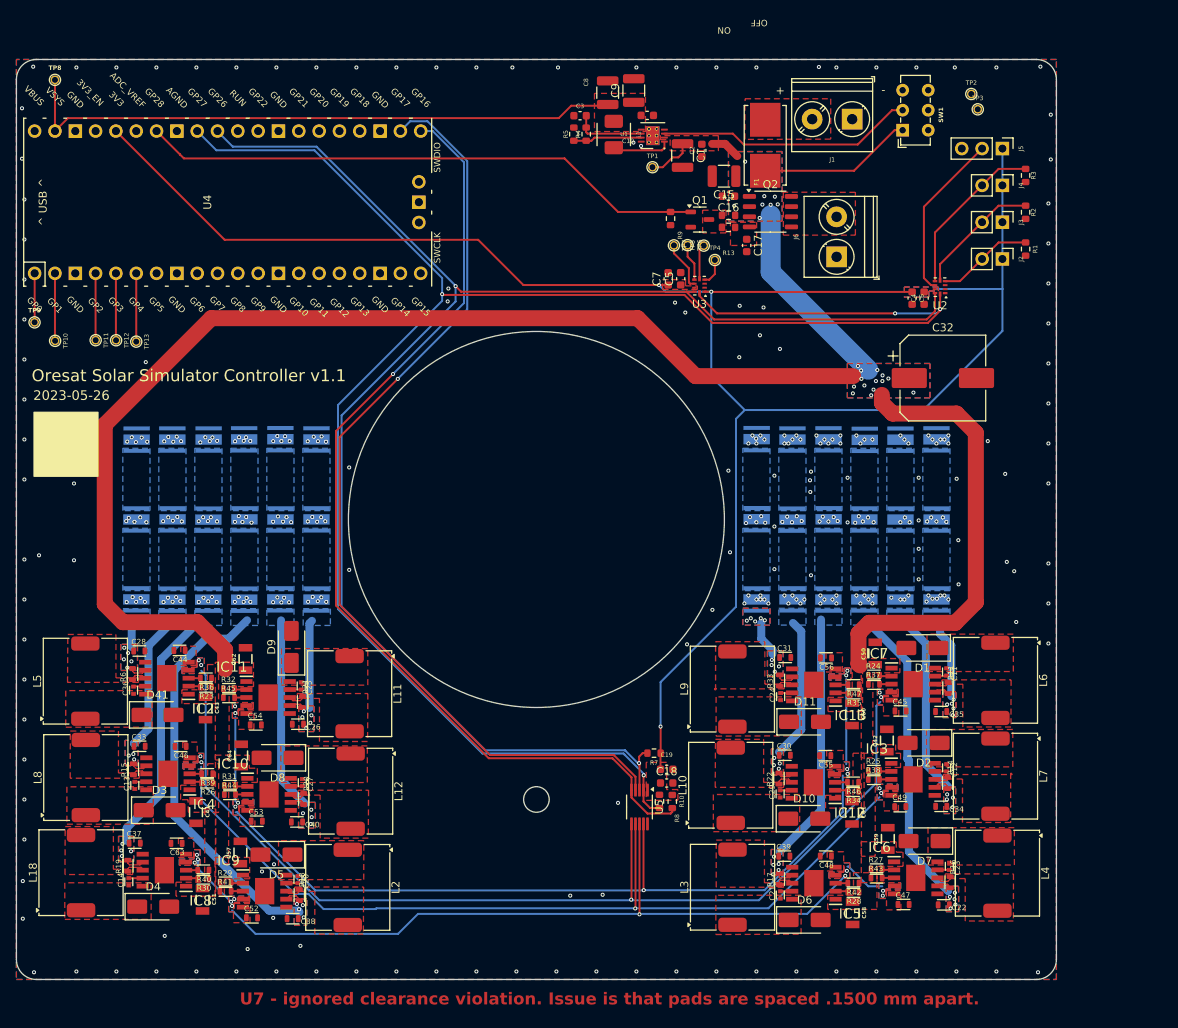
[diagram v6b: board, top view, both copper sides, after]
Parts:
- moved SW1 3.62 mm to (190.8, 53.8)
- moved C64 1.75 mm to (108.1, 132.0)
- moved C8 0.27 mm to (153.9, 49.1)
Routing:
- net +3.3V: track 234.8 -> 243.0 mm
- net VCC: track 256.7 -> 253.3 mm
- net Net-(SW1-B): track 29.7 -> 32.1 mm
- added copper zone on B.Cu, net +3.3V
